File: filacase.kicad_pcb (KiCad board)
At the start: 2 copper layers, 86 x 50 mm, 43 parts, among them J1 Expansion_2, J2 SDcard, J3 SPI 1, J4 Expansion_1, J5 SPI 2, J6 Serial TAG, J7 I2C, J8 +5V, J9 dbg/download port, M2 MountingHole_2.2mm_M2_Pad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

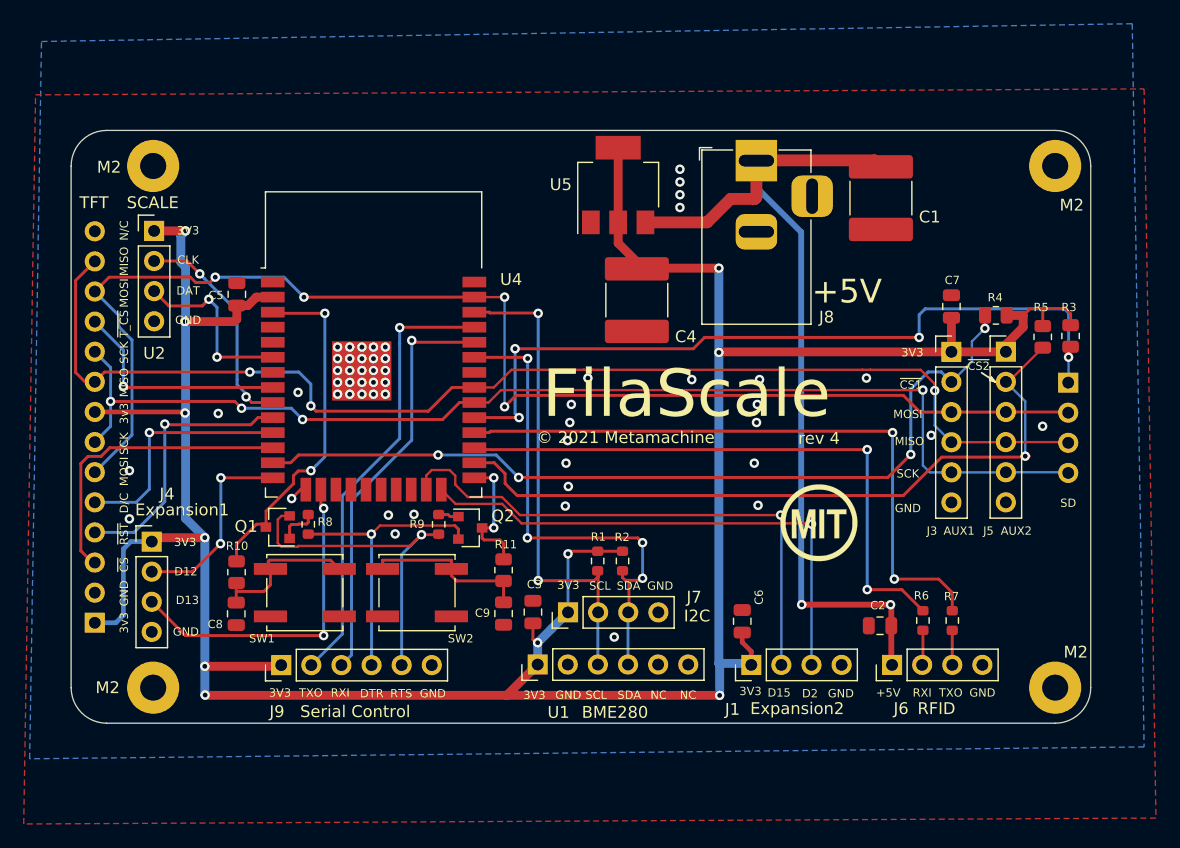
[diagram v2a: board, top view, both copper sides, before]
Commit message: Flipped the display connector and SDCARD connector pads because flipping the connectors to the back of the board also flipped the pins up/down.
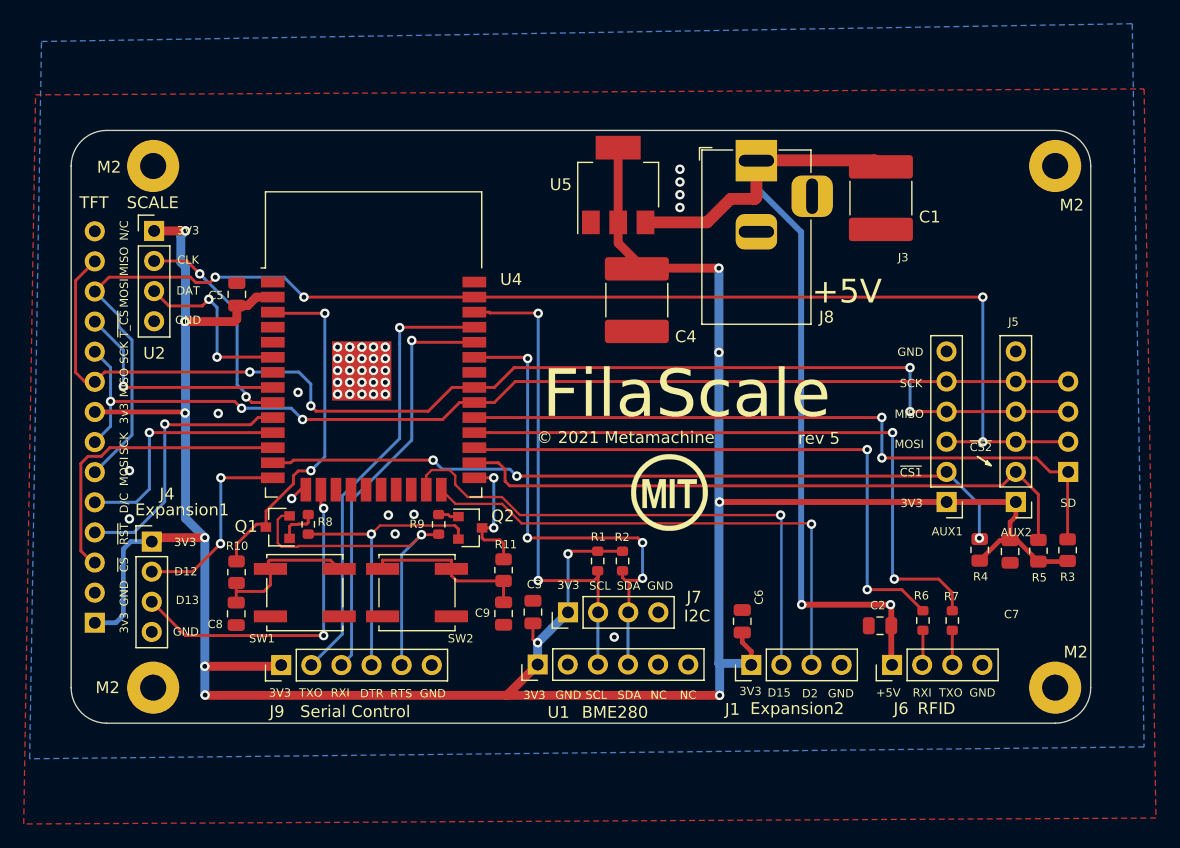
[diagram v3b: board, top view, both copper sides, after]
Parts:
- moved C7 21.3 mm to (137.2, 126.5), turned to 270 degrees
- moved R4 19.8 mm to (134.6, 126.4), turned to 90 degrees
- moved R3 18.1 mm to (142.0, 126.4), turned to 90 degrees
- moved R5 18.0 mm to (139.6, 126.5), turned to 90 degrees
- moved G*** 12.9 mm to (108.5, 121.5)
- moved J5 12.7 mm to (137.7, 122.3), turned to 180 degrees
- moved J3 12.7 mm to (131.8, 122.3), turned to 180 degrees
- moved J2 7.53 mm to (142.1, 119.8), turned to 0 degrees
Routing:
- net /~AUX1_CS~: track 72.4 -> 64.4 mm, vias 4 -> 3
- net /~AUX2_CS~: track 61.2 -> 54.1 mm, vias 1 -> 0
- net /SPI_SCK: track 97.8 -> 91.5 mm, vias 4 -> 3
- net /~SD_CS~: track 65.8 -> 59.7 mm, vias 4 -> 2
- net /SPI_MOSI: track 111.8 -> 116.8 mm
- net +3V3: track 245.1 -> 243.4 mm, vias 11 -> 12
- net /SPI_MISO: track 103.0 -> 102.2 mm, vias 3 -> 4
- net GND: vias 54 -> 38
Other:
- board text added: "rev 5"
- board text removed: "rev 4"

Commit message: Generate a new render of the board; move a couple of traces and rebuild the pours
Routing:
- net GND: vias 38 -> 41
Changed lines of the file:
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@@
     (thickness 1.6)
     (drawings 85)
-    (tracks 485)
+    (tracks 488)
     (zones 0)
     (modules 43)
@@
   (via (at 77.1395 113.096) (size 0.8) (drill 0.4) (layers F.Cu B.Cu) (net 2))
   (via (at 103.8095 133.7335) (size 0.8) (drill 0.4) (layers F.Cu B.Cu) (net 2))
+  (via (at 101.5362 122.24) (size 0.8) (drill 0.4) (layers F.Cu B.Cu) (net 2))
+  (via (at 103.0602 118.9126) (size 0.8) (drill 0.4) (layers F.Cu B.Cu) (net 2))
+  (via (at 134.861 119.8778) (size 0.8) (drill 0.4) (layers F.Cu B.Cu) (net 2))
   (via (at 62.4075 112.588) (size 0.8) (drill 0.4) (layers F.Cu B.Cu) (net 6))
   (segment (start 75.01 112.68) (end 62.4995 112.68) (width 0.25) (layer F.Cu) (net 6))
